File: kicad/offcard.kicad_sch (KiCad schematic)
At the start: 30 parts, among them J10 lower fan, J4 heater, J5 5kg load cell, J6 LCD, J7 upper fan, J8 motor, M1 Motor_DC, U2 IRLML2502TRPBF, U3 NAU7802SGI

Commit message: change 330 ohm resistors to 1206
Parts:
- R12, R2: footprint Resistor_SMD:R_0805_2012Metric_Pad1.20x1.40mm_HandSolder -> Resistor_SMD:R_1206_3216Metric_Pad1.30x1.75mm_HandSolder
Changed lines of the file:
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@@
 			)
 		)
-		(property "Footprint" "Resistor_SMD:R_0805_2012Metric_Pad1.20x1.40mm_HandSolder"
+		(property "Footprint" "Resistor_SMD:R_1206_3216Metric_Pad1.30x1.75mm_HandSolder"
 			(at 35.56 122.428 90)
 			(effects
@@
 			)
 		)
-		(property "Footprint" "Resistor_SMD:R_0805_2012Metric_Pad1.20x1.40mm_HandSolder"
+		(property "Footprint" "Resistor_SMD:R_1206_3216Metric_Pad1.30x1.75mm_HandSolder"
 			(at 121.92 55.118 90)
 			(effects

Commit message: [pcb] swap mosfet inputs
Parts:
- M1: value Motor_DC -> 12VDC motor
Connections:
- net GND: now also U2.2 (S); no longer U2.1 (G)
- net at R12.2: now also U2.1 (G); no longer U2.2 (S)
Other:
- moved on the sheet: R12, R7
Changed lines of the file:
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@@
 	(title_block
 		(title "dankdryer")
-		(date "2025-03-12")
-		(rev "2.0.1")
+		(date "2025-03-18")
+		(rev "2.1.0")
 		(company "dirty south supercomputing")
 		(comment 1 "nick black")
@@
 	)
 	(junction
-		(at 66.04 48.26)
+		(at 110.49 50.8)
 		(diameter 0)
 		(color 0 0 0 0)
 	)
 	(junction
-		(at 33.02 41.91)
+		(at 66.04 48.26)
 		(diameter 0)
 		(color 0 0 0 0)
 	)
 	(junction
-		(at 110.49 53.34)
+		(at 33.02 41.91)
 		(diameter 0)
 		(color 0 0 0 0)
@@
 	(wire
 		(pts
-			(xy 121.92 50.8) (xy 125.73 50.8)
-		)
-		(stroke
-			(width 0)
-			(type default)
-		)
-	)
-	(wire
-		(pts
 			(xy 114.3 134.62) (xy 114.3 125.73)
 		)
@@
 	(wire
 		(pts
-			(xy 106.68 53.34) (xy 110.49 53.34)
-		)
-		(stroke
-			(width 0)
-			(type default)
-		)
-	)
-	(wire
-		(pts
 			(xy 201.93 35.56) (xy 205.74 35.56)
 		)
@@
 	(wire
 		(pts
+			(xy 106.68 50.8) (xy 110.49 50.8)
+		)
+		(stroke
+			(width 0)
+			(type default)
+		)
+	)
+	(wire
+		(pts
 			(xy 30.48 33.02) (xy 30.48 58.42)
 		)
@@
 	(wire
 		(pts
-			(xy 110.49 53.34) (xy 118.11 53.34)
+			(xy 110.49 50.8) (xy 118.11 50.8)
 		)
 		(stroke
@@
 		)
 	)
+	(hierarchical_label "MotorPin"
+		(shape input)
+		(at 106.68 50.8 180)
+		(effects
+			(font
+				(size 1.27 1.27)
+			)
+			(justify right)
+		)
+	)
 	(hierarchical_label "ACNeutral"
 		(shape input)
@@
 		)
 	)
-	(hierarchical_label "MotorPin"
-		(shape input)
-		(at 106.68 53.34 180)
-		(effects
-			(font
-				(size 1.27 1.27)
-			)
-			(justify right)
-		)
-	)
 	(hierarchical_label "ACNeutral"
 		(shape input)
@@
 	(symbol
 		(lib_id "power:GND")
-		(at 121.92 50.8 0)
-		(mirror x)
+		(at 125.73 53.34 0)
+		(mirror y)
 		(unit 1)
 		(exclude_from_sim no)
@@
 		(fields_autoplaced yes)
 		(property "Reference" "#PWR022"
-			(at 121.92 44.45 0)
+			(at 125.73 59.69 0)
 			(effects
 				(font
@@
 		)
 		(property "Value" "GND"
-			(at 119.38 49.5299 0)
+			(at 125.73 58.42 0)
 			(effects
 				(font
 					(size 1.27 1.27)
 				)
-				(justify right)
 			)
 		)
 		(property "Footprint" ""
-			(at 121.92 50.8 0)
+			(at 125.73 53.34 0)
 			(effects
 				(font
@@
 		)
 		(property "Datasheet" ""
-			(at 121.92 50.8 0)
+			(at 125.73 53.34 0)
 			(effects
 				(font
@@
 		)
 		(property "Description" "Power symbol creates a global label with name \"GND\" , ground"
-			(at 121.92 50.8 0)
+			(at 125.73 53.34 0)
 			(effects
 				(font
@@
 		)
 		(instances
-			(project ""
+			(project "dankdryer"
 				(path "/0e28ce9c-097a-4614-9b8c-9333a7b96611/2a0e6a8d-8569-4b27-a15d-bed47a66289a"
 					(reference "#PWR022")
@@
 	(symbol
 		(lib_id "Device:R")
-		(at 110.49 57.15 0)
+		(at 110.49 54.61 0)
 		(unit 1)
 		(exclude_from_sim no)
@@
 		(fields_autoplaced yes)
 		(property "Reference" "R7"
-			(at 113.03 55.8799 0)
+			(at 113.03 53.3399 0)
 			(effects
 				(font
@@
 		)
 		(property "Value" "10k"
-			(at 113.03 58.4199 0)
+			(at 113.03 55.8799 0)
 			(effects
 				(font
@@
 		)
 		(property "Footprint" "Resistor_SMD:R_0805_2012Metric_Pad1.20x1.40mm_HandSolder"
-			(at 108.712 57.15 90)
+			(at 108.712 54.61 90)
 			(effects
 				(font
@@
 		)
 		(property "Datasheet" "~"
-			(at 110.49 57.15 0)
+			(at 110.49 54.61 0)
 			(effects
 				(font
@@
 		)
 		(property "Description" "Resistor"
-			(at 110.49 57.15 0)
+			(at 110.49 54.61 0)
 			(effects
 				(font
@@
 		)
 		(instances
-			(project ""
+			(project "dankdryer"
 				(path "/0e28ce9c-097a-4614-9b8c-9333a7b96611/2a0e6a8d-8569-4b27-a15d-bed47a66289a"
 					(reference "R7")
@@
 	(symbol
 		(lib_id "power:GND")
-		(at 110.49 60.96 0)
+		(at 110.49 58.42 0)
 		(unit 1)
 		(exclude_from_sim no)
@@
 		(fields_autoplaced yes)
 		(property "Reference" "#PWR032"
-			(at 110.49 67.31 0)
+			(at 110.49 64.77 0)
 			(effects
 				(font
@@
 		)
 		(property "Value" "GND"
-			(at 110.49 66.04 0)
+			(at 110.49 63.5 0)
 			(effects
 				(font
@@
 		)
 		(property "Footprint" ""
-			(at 110.49 60.96 0)
+			(at 110.49 58.42 0)
 			(effects
 				(font
@@
 		)
 		(property "Datasheet" ""
-			(at 110.49 60.96 0)
+			(at 110.49 58.42 0)
 			(effects
 				(font
@@
 		)
 		(property "Description" "Power symbol creates a global label with name \"GND\" , ground"
-			(at 110.49 60.96 0)
+			(at 110.49 58.42 0)
 			(effects
 				(font
@@
 		(dnp no)
 		(property "Reference" "D2"
-			(at 158.496 64.77 90)
+			(at 158.496 59.69 90)
 			(effects
 				(font
@@
 		)
 		(property "Value" "D_Schottky"
-			(at 155.448 66.802 90)
+			(at 154.686 62.484 90)
 			(effects
 				(font
@@
 	(symbol
 		(lib_id "Device:R")
-		(at 121.92 53.34 90)
+		(at 121.92 50.8 90)
 		(unit 1)
 		(exclude_from_sim no)
@@
 		(dnp no)
 		(property "Reference" "R12"
-			(at 121.92 57.912 90)
+			(at 121.92 55.372 90)
 			(effects
 				(font
@@
 		)
 		(property "Value" "330"
-			(at 121.92 55.88 90)
+			(at 121.92 53.34 90)
 			(effects
 				(font
@@
 		)
 		(property "Footprint" "Resistor_SMD:R_1206_3216Metric_Pad1.30x1.75mm_HandSolder"
-			(at 121.92 55.118 90)
+			(at 121.92 52.578 90)
 			(effects
 				(font
@@
 		)
 		(property "Datasheet" "~"
-			(at 121.92 53.34 0)
+			(at 121.92 50.8 0)
 			(effects
 				(font
@@
 		)
 		(property "Description" "Resistor"
-			(at 121.92 53.34 0)
+			(at 121.92 50.8 0)
 			(effects
 				(font
@@
 		)
 		(instances
-			(project ""
+			(project "dankdryer"
 				(path "/0e28ce9c-097a-4614-9b8c-9333a7b96611/2a0e6a8d-8569-4b27-a15d-bed47a66289a"
 					(reference "R12")
@@
 		(dnp no)
 		(property "Reference" "M1"
-			(at 163.576 61.214 0)
+			(at 164.084 38.354 0)
 			(effects
 				(font
@@
 			)
 		)
-		(property "Value" "Motor_DC"
-			(at 159.766 57.404 0)
+		(property "Value" "12VDC motor"
+			(at 160.782 41.656 0)
 			(effects
 				(font

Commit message: put your boot down
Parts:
- R7: footprint Resistor_SMD:R_0805_2012Metric_Pad1.20x1.40mm_HandSolder -> Resistor_SMD:R_1206_3216Metric_Pad1.30x1.75mm_HandSolder
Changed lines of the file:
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@@
 	(text "0.005A minimum to drive MOC3063SM.\n3.3V / 330Ω = 0.01A (0.033W).\nMOC3063 has drop of 1.3-1.5V, forward current of 60mA.\nHeater neutral returns from 150C thermostat.\nHeater is resistive load, no need for snubber circuit.\n50W±20% max draw -> 60W / 120VAC -> 0.5A max switched in triac.\nT1210 wants 1.3V and latching 25-30mA / holding 15mA (max 0.039W),\n switches 12A continuous and 126A peak of 120VAC@60Hz.\nRK73H2As support 150V and 0.25W."
 		(exclude_from_sim no)
-		(at 15.24 161.29 0)
+		(at 16.51 159.766 0)
 		(effects
 			(font
@@
 		(stroke
 			(width 0)
-			(type default)
+			(type solid)
 		)
 		(fill
-			(type none)
+			(type color)
+			(color 241 209 255 1)
 		)
 		(effects
@@
 		)
 	)
-	(global_label "UPWM"
-		(shape input)
-		(at 36.83 45.72 0)
-		(fields_autoplaced yes)
-		(effects
-			(font
-				(size 1.27 1.27)
-			)
-			(justify left)
-		)
-		(property "Intersheetrefs" "${INTERSHEET_REFS}"
-			(at 45.3185 45.72 0)
-			(effects
-				(font
-					(size 1.27 1.27)
-				)
-				(justify left)
-				(hide yes)
-			)
-		)
-	)
 	(global_label "LCDSCL"
 		(shape input)
@@
 		)
 	)
-	(global_label "LTach"
+	(global_label "A+"
 		(shape input)
-		(at 66.04 67.31 0)
+		(at 227.33 76.2 0)
 		(fields_autoplaced yes)
 		(effects
@@
 		)
 		(property "Intersheetrefs" "${INTERSHEET_REFS}"
-			(at 74.4075 67.31 0)
+			(at 232.9762 76.2 0)
 			(effects
 				(font
@@
 		)
 	)
-	(global_label "LPWM"
+	(global_label "A-"
 		(shape input)
-		(at 63.5 45.72 180)
+		(at 227.33 78.74 0)
 		(fields_autoplaced yes)
 		(effects
@@
 				(size 1.27 1.27)
 			)
-			(justify right)
+			(justify left)
 		)
 		(property "Intersheetrefs" "${INTERSHEET_REFS}"
-			(at 55.3139 45.72 0)
-			(effects
-				(font
-					(size 1.27 1.27)
-				)
-				(justify right)
+			(at 232.9762 78.74 0)
+			(effects
+				(font
+					(size 1.27 1.27)
+				)
+				(justify left)
 				(hide yes)
 			)
@@
 		)
 	)
+	(global_label "A-"
+		(shape input)
+		(at 191.77 35.56 180)
+		(fields_autoplaced yes)
+		(effects
+			(font
+				(size 1.27 1.27)
+			)
+			(justify right)
+		)
+		(property "Intersheetrefs" "${INTERSHEET_REFS}"
+			(at 186.1238 35.56 0)
+			(effects
+				(font
+					(size 1.27 1.27)
+				)
+				(justify right)
+				(hide yes)
+			)
+		)
+	)
+	(global_label "A+"
+		(shape input)
+		(at 191.77 44.45 180)
+		(fields_autoplaced yes)
+		(effects
+			(font
+				(size 1.27 1.27)
+			)
+			(justify right)
+		)
+		(property "Intersheetrefs" "${INTERSHEET_REFS}"
+			(at 186.1238 44.45 0)
+			(effects
+				(font
+					(size 1.27 1.27)
+				)
+				(justify right)
+				(hide yes)
+			)
+		)
+	)
 	(global_label "LCDDC"
 		(shape input)
@@
 		)
 	)
-	(global_label "UTach"
+	(hierarchical_label "UTach"
 		(shape input)
 		(at 33.02 67.31 180)
-		(fields_autoplaced yes)
 		(effects
 			(font
@@
 			)
 			(justify right)
-		)
-		(property "Intersheetrefs" "${INTERSHEET_REFS}"
-			(at 24.3501 67.31 0)
-			(effects
-				(font
-					(size 1.27 1.27)
-				)
-				(justify right)
-				(hide yes)
-			)
 		)
 	)
@@
 		)
 	)
-	(hierarchical_label "A-"
+	(hierarchical_label "LTach"
 		(shape input)
-		(at 227.33 78.74 0)
+		(at 66.04 67.31 0)
 		(effects
 			(font
@@
 			)
 			(justify left)
-		)
-	)
-	(hierarchical_label "A+"
-		(shape input)
-		(at 191.77 44.45 180)
-		(effects
-			(font
-				(size 1.27 1.27)
-			)
-			(justify right)
 		)
 	)
@@
 		)
 	)
-	(hierarchical_label "A+"
+	(hierarchical_label "UPWM"
 		(shape input)
-		(at 227.33 76.2 0)
+		(at 36.83 45.72 0)
 		(effects
 			(font
@@
 		)
 	)
+	(hierarchical_label "LPWM"
+		(shape input)
+		(at 63.5 45.72 180)
+		(effects
+			(font
+				(size 1.27 1.27)
+			)
+			(justify right)
+		)
+	)
 	(hierarchical_label "HeaterNeutral"
 		(shape input)
@@
 			)
 			(justify left)
-		)
-	)
-	(hierarchical_label "A-"
-		(shape input)
-		(at 191.77 35.56 180)
-		(effects
-			(font
-				(size 1.27 1.27)
-			)
-			(justify right)
 		)
 	)
@@
 			)
 		)
-		(property "Footprint" "Resistor_SMD:R_0805_2012Metric_Pad1.20x1.40mm_HandSolder"
+		(property "Footprint" "Resistor_SMD:R_1206_3216Metric_Pad1.30x1.75mm_HandSolder"
 			(at 108.712 54.61 90)
 			(effects

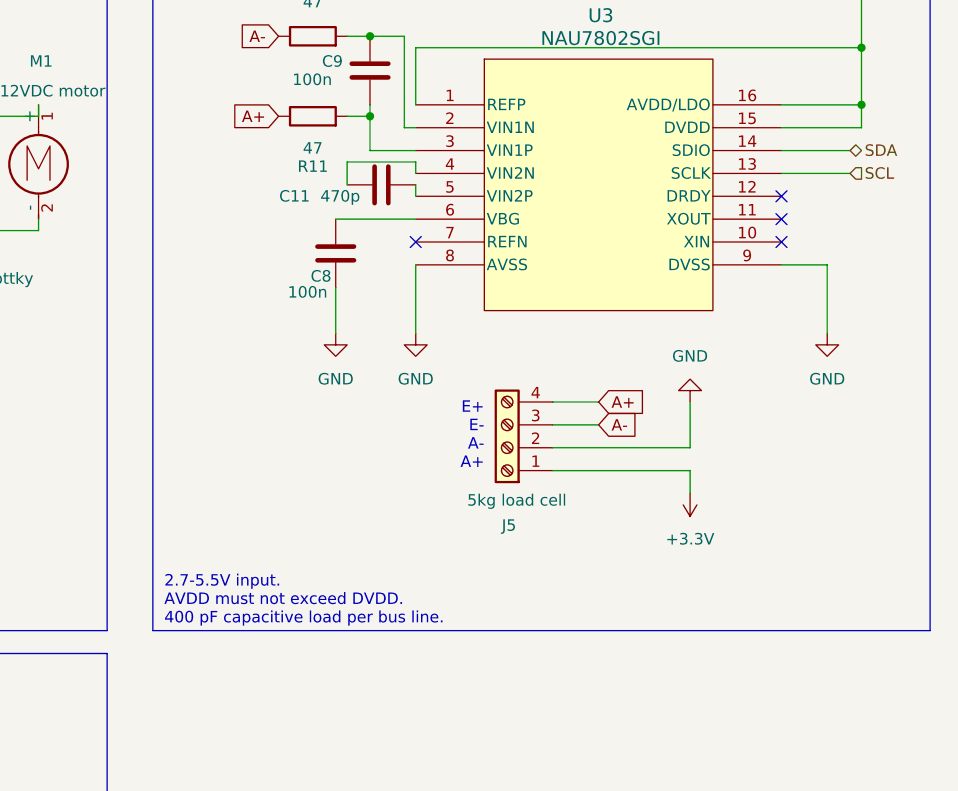
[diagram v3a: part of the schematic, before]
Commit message: move to 2.2k resistors for I2C
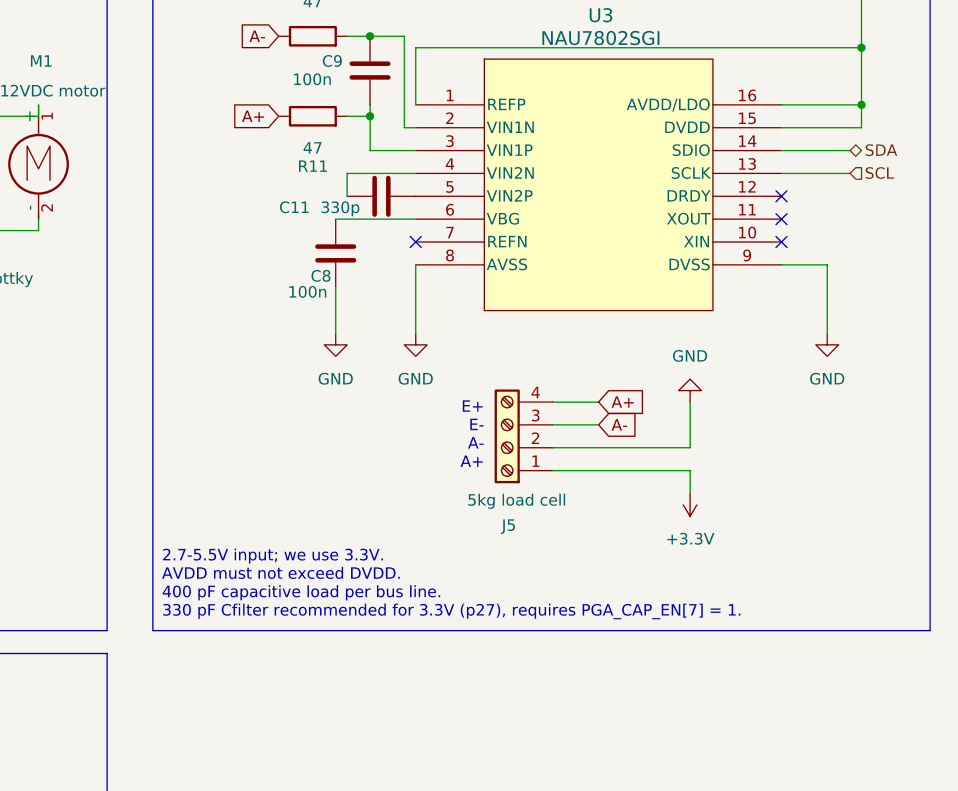
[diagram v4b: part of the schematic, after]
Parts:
- C11: value 470p -> 330p
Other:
- note added: "2.7-5.5V input; we use 3.3V. AVDD must not exceed DVDD. 400 pF capacitive load per bus line. 330 pF Cfilter recommended for 3.3V (p27), requires PGA_CAP_EN[7] = 1."
- note removed: "2.7-5.5V input. AVDD must not exceed DVDD. 400 pF capacitive load per bus line."
- moved on the sheet: C11
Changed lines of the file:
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@@
 		)
 	)
-	(text "2.7-5.5V input.\nAVDD must not exceed DVDD.\n400 pF capacitive load per bus line."
+	(text "2.7-5.5V input; we use 3.3V.\nAVDD must not exceed DVDD.\n400 pF capacitive load per bus line.\n330 pF Cfilter recommended for 3.3V (p27), requires PGA_CAP_EN[7] = 1."
 		(exclude_from_sim no)
-		(at 179.07 98.298 0)
+		(at 178.816 96.52 0)
 		(effects
 			(font
@@
 	(wire
 		(pts
-			(xy 207.01 49.53) (xy 199.39 49.53)
+			(xy 207.01 50.8) (xy 199.39 50.8)
 		)
 		(stroke
@@
 	(wire
 		(pts
-			(xy 207.01 52.07) (xy 207.01 53.34)
-		)
-		(stroke
-			(width 0)
-			(type default)
-		)
-	)
-	(wire
-		(pts
 			(xy 52.07 130.81) (xy 48.26 130.81)
 		)
@@
 	(wire
 		(pts
-			(xy 199.39 49.53) (xy 199.39 52.07)
-		)
-		(stroke
-			(width 0)
-			(type default)
-		)
-	)
-	(wire
-		(pts
-			(xy 207.01 50.8) (xy 207.01 49.53)
+			(xy 199.39 50.8) (xy 199.39 53.34)
 		)
 		(stroke
@@
 	(symbol
 		(lib_id "Device:C")
-		(at 203.2 52.07 90)
+		(at 203.2 53.34 90)
 		(unit 1)
 		(exclude_from_sim no)
@@
 		(dnp no)
 		(property "Reference" "C11"
-			(at 193.548 53.34 90)
-			(effects
-				(font
-					(size 1.27 1.27)
-				)
-			)
-		)
-		(property "Value" "470p"
-			(at 198.628 53.34 90)
+			(at 193.548 54.61 90)
+			(effects
+				(font
+					(size 1.27 1.27)
+				)
+			)
+		)
+		(property "Value" "330p"
+			(at 198.628 54.61 90)
 			(effects
 				(font
@@
 		)
 		(property "Footprint" "Capacitor_SMD:C_0805_2012Metric_Pad1.18x1.45mm_HandSolder"
-			(at 207.01 51.1048 0)
+			(at 207.01 52.3748 0)
 			(effects
 				(font
@@
 		)
 		(property "Datasheet" "~"
-			(at 203.2 52.07 0)
+			(at 203.2 53.34 0)
 			(effects
 				(font
@@
 		)
 		(property "Description" "Unpolarized capacitor"
-			(at 203.2 52.07 0)
-			(effects
-				(font
+			(at 203.2 53.34 0)
+			(effects
+				(font
